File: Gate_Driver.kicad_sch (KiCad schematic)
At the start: 27 parts, among them U1 DRV8323RSRGZR

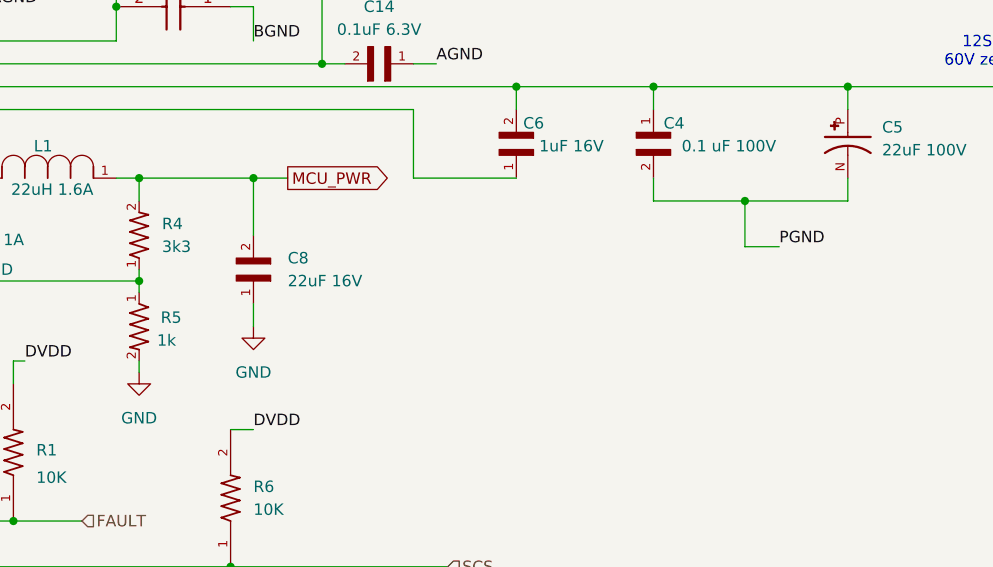
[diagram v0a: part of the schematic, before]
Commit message: Footprints prepared, first pcb project created.
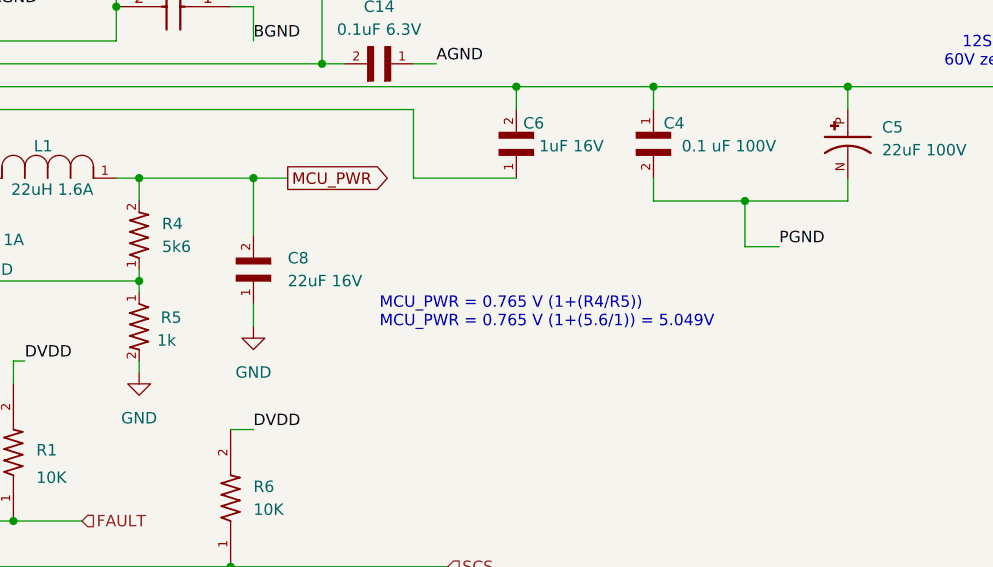
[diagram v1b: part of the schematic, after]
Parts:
- C1, C3: footprint C0805 -> Capacitor_SMD:C_0805_2012Metric_Pad1.18x1.45mm_HandSolder
- C2: footprint CAPC1005X55N -> Capacitor_SMD:C_0603_1608Metric_Pad1.08x0.95mm_HandSolder
- R4: value 3k3 -> 5k6
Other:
- note added: "MCU_PWR = 0.765 V (1+(R4/R5)) MCU_PWR = 0.765 V (1+(5.6/1)) = 5.049V"
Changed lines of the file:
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@@
 		(rev "v0.1")
 	)
+	(text " MCU_PWR = 0.765 V (1+(R4/R5))\n MCU_PWR = 0.765 V (1+(5.6/1)) = 5.049V"
+		(exclude_from_sim no)
+		(at 158.242 74.676 0)
+		(effects
+			(font
+				(size 1.27 1.27)
+			)
+			(justify left)
+		)
+	)
 	(text "MCU must sense the\nvoltage at each phase\nfor 6-step algorithm\n"
 		(exclude_from_sim no)
@@
 			)
 		)
-		(property "Footprint" "CAPC1005X55N"
+		(property "Footprint" "Capacitor_SMD:C_0603_1608Metric_Pad1.08x0.95mm_HandSolder"
 			(at 104.14 -59.36 0)
 			(effects
@@
 			)
 		)
-		(property "Footprint" "C0805"
+		(property "Footprint" "Capacitor_SMD:C_0805_2012Metric_Pad1.18x1.45mm_HandSolder"
 			(at 138.1 121.92 0)
 			(effects
@@
 			)
 		)
-		(property "Footprint" "C0805"
+		(property "Footprint" "Capacitor_SMD:C_0805_2012Metric_Pad1.18x1.45mm_HandSolder"
 			(at 133.35 -55.55 0)
 			(effects
@@
 			)
 		)
-		(property "Value" "3k3"
+		(property "Value" "5k6"
 			(at 134.62 67.3099 90)
 			(effects

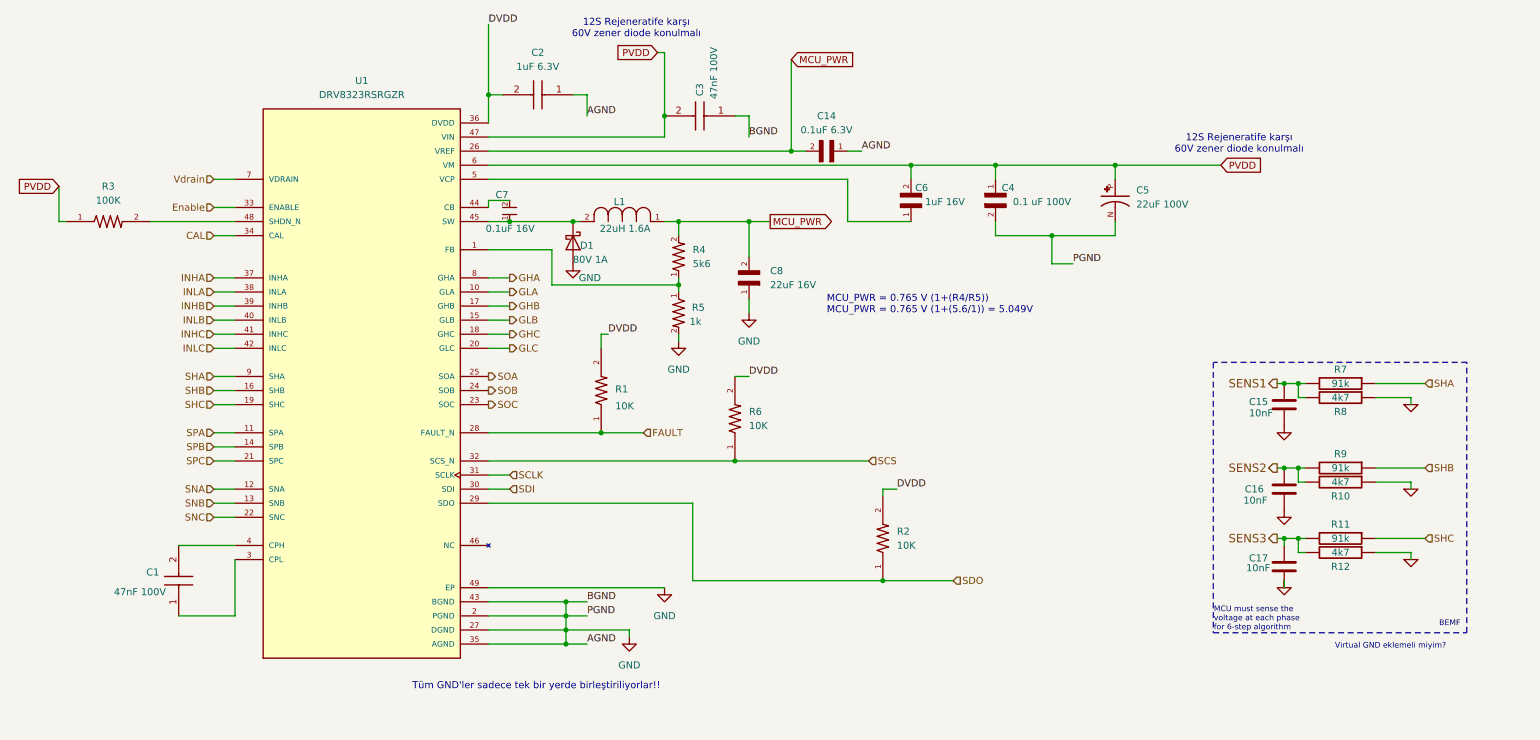
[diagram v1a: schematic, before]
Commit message: component list updated, all footprints updated and now they are compatible to produce with hand (no 0402 size)
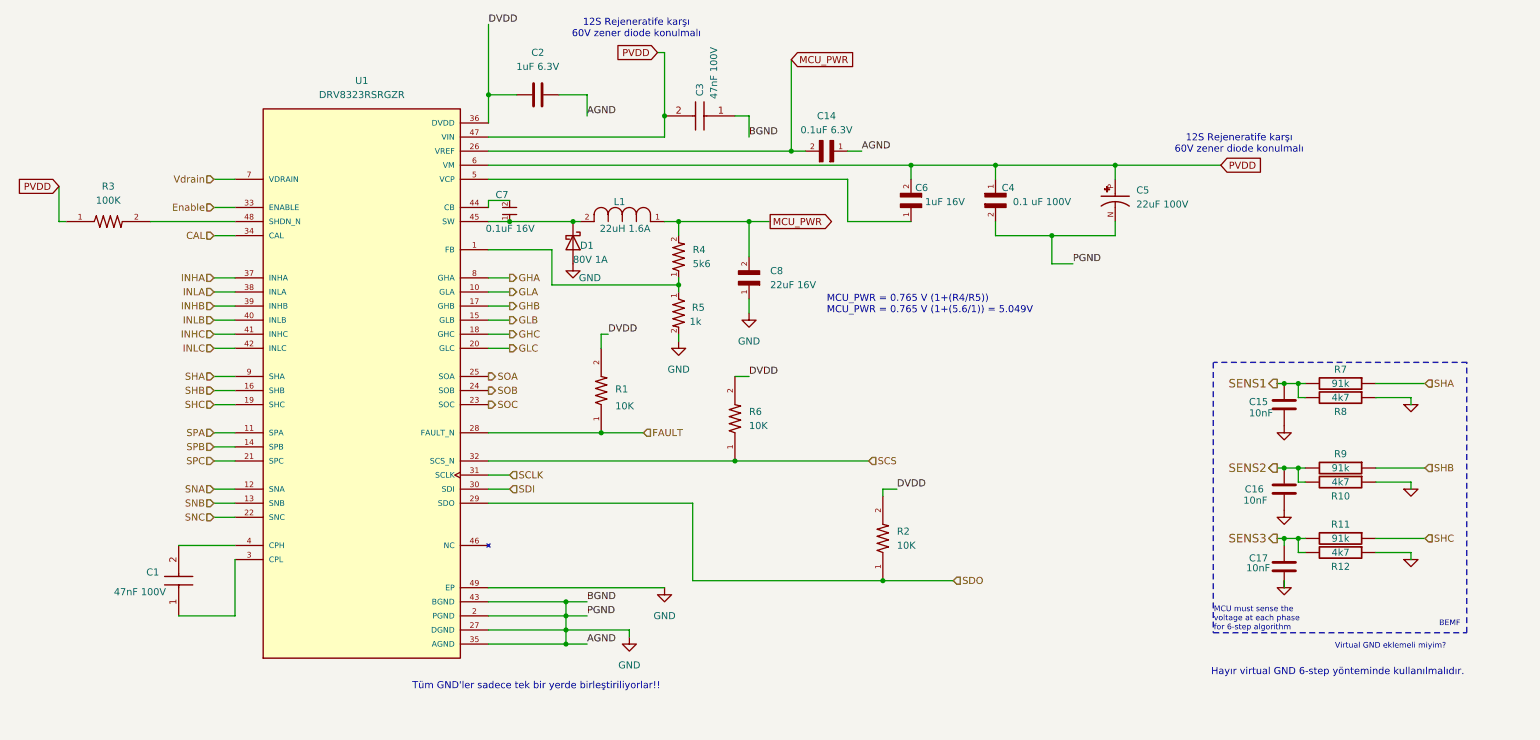
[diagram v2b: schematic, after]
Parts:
- removed C2: 1uF 6.3V, Capacitor_SMD:C_0603_1608Metric_Pad1.08x0.95mm_HandSolder, symbol CL05B105KQ5NQNC:CL05B105KQ5NQNC
- added C2: 1uF 6.3V, Capacitor_SMD:C_0603_1608Metric_Pad1.08x0.95mm_HandSolder, symbol Device:C
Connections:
- net DVDD: now also C2.1
- net GND: now also C2.2
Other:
- note added: "Hayır virtual GND 6-step yönteminde kullanılmalıdır."
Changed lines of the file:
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@@
 		)
 	)
+	(text "Hayır virtual GND 6-step yönteminde kullanılmalıdır."
+		(exclude_from_sim no)
+		(at 250.952 140.97 0)
+		(effects
+			(font
+				(size 1.27 1.27)
+			)
+		)
+	)
 	(text "MCU must sense the\nvoltage at each phase\nfor 6-step algorithm\n"
 		(exclude_from_sim no)
@@
 	(wire
 		(pts
-			(xy 97.79 36.83) (xy 100.33 36.83)
+			(xy 97.79 36.83) (xy 102.87 36.83)
 		)
 		(stroke
@@
 	(wire
 		(pts
-			(xy 113.03 36.83) (xy 115.57 36.83)
-		)
-		(stroke
-			(width 0)
-			(type default)
-		)
-	)
-	(wire
-		(pts
 			(xy 257.81 91.44) (xy 264.16 91.44)
 		)
@@
 	(wire
 		(pts
+			(xy 110.49 36.83) (xy 115.57 36.83)
+		)
+		(stroke
+			(width 0)
+			(type default)
+		)
+	)
+	(wire
+		(pts
 			(xy 48.26 102.87) (xy 52.07 102.87)
 		)
@@
 	)
 	(symbol
-		(lib_id "CL05B105KQ5NQNC:CL05B105KQ5NQNC")
-		(at 113.03 36.83 180)
+		(lib_id "Device:C")
+		(at 106.68 36.83 90)
 		(unit 1)
 		(exclude_from_sim no)
@@
 		(fields_autoplaced yes)
 		(property "Reference" "C2"
-			(at 106.68 29.21 0)
+			(at 106.68 29.21 90)
 			(effects
 				(font
@@
 		)
 		(property "Value" "1uF 6.3V"
-			(at 106.68 31.75 0)
+			(at 106.68 31.75 90)
 			(effects
 				(font
@@
 		)
 		(property "Footprint" "Capacitor_SMD:C_0603_1608Metric_Pad1.08x0.95mm_HandSolder"
-			(at 104.14 -59.36 0)
+			(at 110.49 35.8648 0)
 			(effects
 				(font
 					(size 1.27 1.27)
 				)
-				(justify left top)
 				(hide yes)
 			)
 		)
-		(property "Datasheet" "https://media.digikey.com/pdf/Data%20Sheets/Samsung%20PDFs/CL10A225KO8NNNC_Spec.pdf"
-			(at 104.14 -159.36 0)
+		(property "Datasheet" "https://www.direnc.net/1uf-16v-10-x5r-603-smd-kondansator"
+			(at 106.68 36.83 0)
 			(effects
 				(font
 					(size 1.27 1.27)
 				)
-				(justify left top)
 				(hide yes)
 			)
 		)
-		(property "Description" "Cap Ceramic 1uF 6.3V X7R 10% Pad SMD 0402 125C T/R"
-			(at 113.03 36.83 0)
+		(property "Description" "Unpolarized capacitor ()"
+			(at 106.68 36.83 0)
 			(effects
 				(font
@@
 			)
 		)
-		(property "Height" "0.55"
-			(at 104.14 -359.36 0)
-			(effects
-				(font
-					(size 1.27 1.27)
-				)
-				(justify left top)
-				(hide yes)
-			)
-		)
-		(property "Manufacturer_Name" "SAMSUNG"
-			(at 104.14 -459.36 0)
-			(effects
-				(font
-					(size 1.27 1.27)
-				)
-				(justify left top)
-				(hide yes)
-			)
-		)
-		(property "Manufacturer_Part_Number" "CL05B105KQ5NQNC"
-			(at 104.14 -559.36 0)
-			(effects
-				(font
-					(size 1.27 1.27)
-				)
-				(justify left top)
-				(hide yes)
-			)
-		)
-		(property "Mouser Part Number" "187-CL05B105KQ5NQNC"
-			(at 104.14 -659.36 0)
-			(effects
-				(font
-					(size 1.27 1.27)
-				)
-				(justify left top)
-				(hide yes)
-			)
-		)
-		(property "Mouser Price/Stock" "https://www.mouser.co.uk/ProductDetail/Samsung-Electro-Mechanics/CL05B105KQ5NQNC?qs=rzUXcgKXlodZ31DFWLtHjw%3D%3D"
-			(at 104.14 -759.36 0)
-			(effects
-				(font
-					(size 1.27 1.27)
-				)
-				(justify left top)
-				(hide yes)
-			)
-		)
-		(property "Arrow Part Number" "CL05B105KQ5NQNC"
-			(at 104.14 -859.36 0)
-			(effects
-				(font
-					(size 1.27 1.27)
-				)
-				(justify left top)
-				(hide yes)
-			)
-		)
-		(property "Arrow Price/Stock" "https://www.arrow.com/en/products/cl05b105kq5nqnc/samsung-electro-mechanics?region=nac"
-			(at 104.14 -959.36 0)
-			(effects
-				(font
-					(size 1.27 1.27)
-				)
-				(justify left top)
-				(hide yes)
-			)
-		)
 		(pin "1"
 		)
@@
 			)
 		)
-		(property "Datasheet" ""
+		(property "Datasheet" "kicad-embed://drv8323.pdf"
 			(at 74.93 87.63 0)
 			(effects

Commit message: some tags chaneged, pcb thinked about pcb component placement, aluminum mosfet carrier pcb and paralelling mosfets
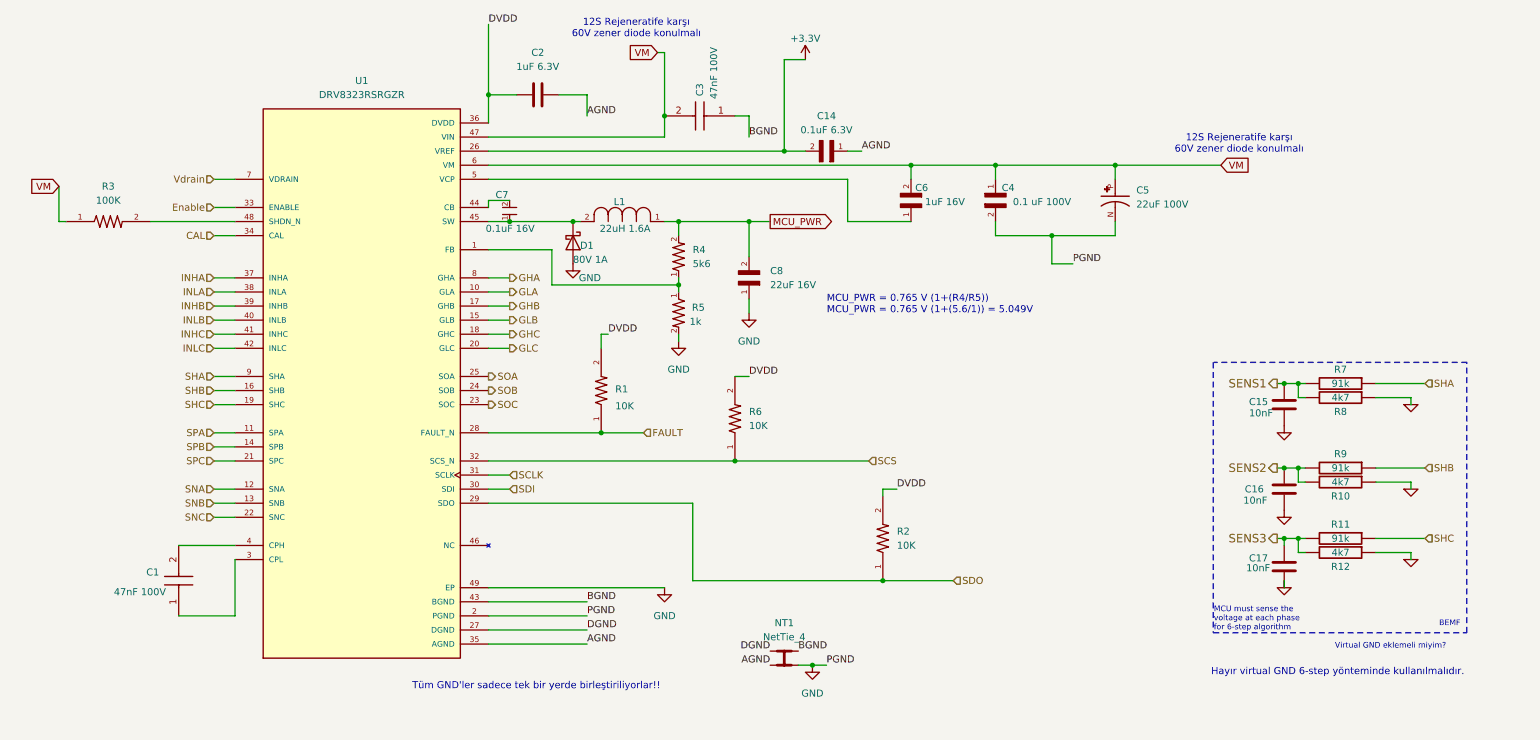
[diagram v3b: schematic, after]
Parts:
- added NT1: NetTie_4, symbol Device:NetTie_4
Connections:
- net GND: now also NT1.4; no longer C14.1, C2.2, C3.1, U1.27 (DGND), U1.35 (AGND), U1.43 (BGND)
- net MCU_PWR: no longer C14.2, U1.26 (VREF)
- net PVDD renamed VM
- new net +3.3V: C14.2, U1.26 (VREF)
- new net AGND: C14.1, C2.2, NT1.3, U1.35 (AGND)
- new net BGND: C3.1, NT1.2, U1.43 (BGND)
- new net DGND: NT1.1, U1.27 (DGND)

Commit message: d;akljadsl;kdsj
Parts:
- C7: footprint CC0603KRX7R7BB104:CAPC1608X90 -> Capacitor_SMD:C_0603_1608Metric_Pad1.08x0.95mm_HandSolder
- C8: footprint CL21A226KOQNNNE:CAPC2012X140N -> Capacitor_SMD:C_0805_2012Metric_Pad1.18x1.45mm_HandSolder
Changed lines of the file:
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@@
 			)
 		)
-		(property "Footprint" "CC0603KRX7R7BB104:CAPC1608X90"
+		(property "Footprint" "Capacitor_SMD:C_0603_1608Metric_Pad1.08x0.95mm_HandSolder"
 			(at 119.888 44.704 0)
 			(effects
@@
 			)
 		)
-		(property "Footprint" "CL21A226KOQNNNE:CAPC2012X140N"
+		(property "Footprint" "Capacitor_SMD:C_0805_2012Metric_Pad1.18x1.45mm_HandSolder"
 			(at 144.78 71.12 0)
 			(effects

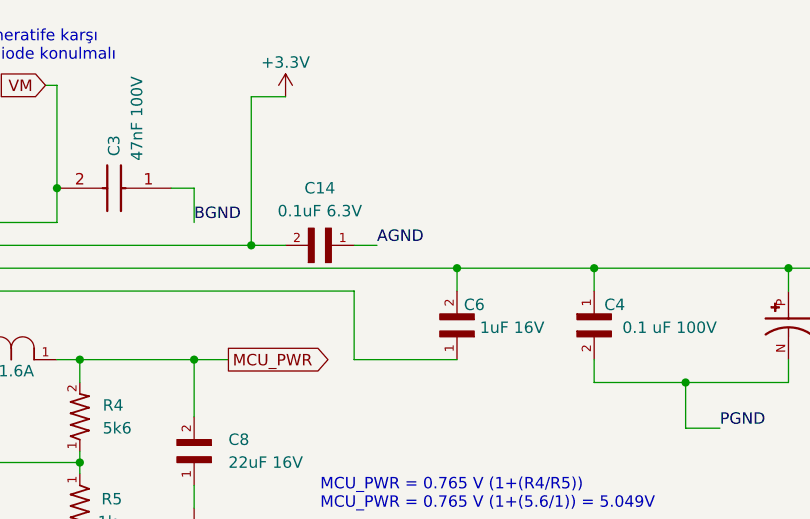
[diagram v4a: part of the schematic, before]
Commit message: started to pcb design, mosfets,shunts drv8323 placement.
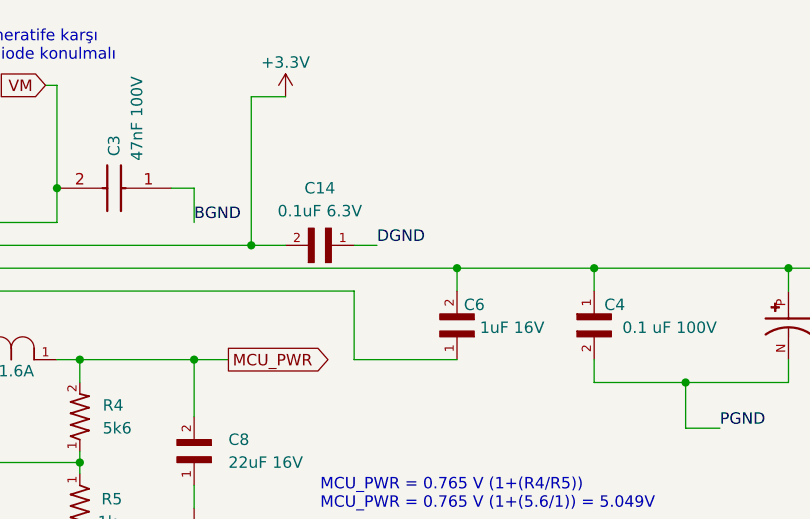
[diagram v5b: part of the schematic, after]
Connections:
- net AGND: no longer C14.1
- net DGND: now also C14.1
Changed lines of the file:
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@@
 		)
 	)
-	(label "AGND"
+	(label "DGND"
 		(at 165.1 46.99 0)
 		(effects

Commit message: all nıght 4/12
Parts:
- removed NT1: NetTie_4, symbol Device:NetTie_4
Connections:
- net GND: no longer C4.2, C5.N, U1.2 (PGND)
- new net PGND: C4.2, C5.N, U1.2 (PGND)
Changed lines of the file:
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@@
 	)
 	(junction
-		(at 156.21 139.7)
-		(diameter 0)
-		(color 0 0 0 0)
-	)
-	(junction
 		(at 243.84 88.9)
 		(diameter 0)
@@
 	(wire
 		(pts
-			(xy 97.79 130.81) (xy 115.57 130.81)
-		)
-		(stroke
-			(width 0)
-			(type default)
-		)
-	)
-	(wire
-		(pts
 			(xy 97.79 72.39) (xy 101.6 72.39)
 		)
@@
 	(wire
 		(pts
-			(xy 97.79 128.27) (xy 115.57 128.27)
-		)
-		(stroke
-			(width 0)
-			(type default)
-		)
-	)
-	(wire
-		(pts
 			(xy 48.26 82.55) (xy 52.07 82.55)
 		)
@@
 		)
 	)
-	(wire
-		(pts
-			(xy 156.21 139.7) (xy 153.67 139.7)
-		)
-		(stroke
-			(width 0)
-			(type default)
-		)
-	)
 	(polyline
 		(pts
@@
 	(wire
 		(pts
+			(xy 97.79 128.27) (xy 115.57 128.27)
+		)
+		(stroke
+			(width 0)
+			(type default)
+		)
+	)
+	(wire
+		(pts
 			(xy 97.79 49.53) (xy 173.99 49.53)
 		)
@@
 	(wire
 		(pts
-			(xy 158.75 139.7) (xy 156.21 139.7)
+			(xy 97.79 130.81) (xy 115.57 130.81)
 		)
 		(stroke
@@
 		)
 	)
-	(label "AGND"
-		(at 148.59 139.7 180)
-		(effects
-			(font
-				(size 1.27 1.27)
-			)
-			(justify right bottom)
-		)
-	)
 	(label "PGND"
 		(at 115.57 130.81 0)
@@
 		)
 	)
-	(label "PGND"
-		(at 158.75 139.7 0)
-		(effects
-			(font
-				(size 1.27 1.27)
-			)
-			(justify left bottom)
-		)
-	)
 	(label "DGND"
 		(at 165.1 46.99 0)
@@
 		)
 	)
-	(label "DGND"
-		(at 148.59 137.16 180)
-		(effects
-			(font
-				(size 1.27 1.27)
-			)
-			(justify right bottom)
-		)
-	)
 	(label "DVDD"
 		(at 171.45 107.95 0)
@@
 		)
 	)
-	(label "BGND"
-		(at 153.67 137.16 0)
-		(effects
-			(font
-				(size 1.27 1.27)
-			)
-			(justify left bottom)
-		)
-	)
 	(global_label "VM"
 		(shape input)
@@
 	)
 	(symbol
-		(lib_id "Device:NetTie_4")
-		(at 151.13 137.16 0)
-		(unit 1)
-		(exclude_from_sim no)
-		(in_bom no)
-		(on_board yes)
-		(dnp no)
-		(fields_autoplaced yes)
-		(property "Reference" "NT1"
-			(at 151.13 132.08 0)
-			(effects
-				(font
-					(size 1.27 1.27)
-				)
-			)
-		)
-		(property "Value" "NetTie_4"
-			(at 151.13 134.62 0)
-			(effects
-				(font
-					(size 1.27 1.27)
-				)
-			)
-		)
-		(property "Footprint" ""
-			(at 151.13 137.16 0)
-			(effects
-				(font
-					(size 1.27 1.27)
-				)
-				(hide yes)
-			)
-		)
-		(property "Datasheet" "~"
-			(at 151.13 137.16 0)
-			(effects
-				(font
-					(size 1.27 1.27)
-				)
-				(hide yes)
-			)
-		)
-		(property "Description" "Net tie, 4 pins"
-			(at 151.13 137.16 0)
-			(effects
-				(font
-					(size 1.27 1.27)
-				)
-				(hide yes)
-			)
-		)
-		(pin "4"
-		)
-		(pin "3"
-		)
-		(pin "2"
-		)
-		(pin "1"
-		)
-		(instances
-			(project ""
-				(path "/57129761-6d47-486c-bd7a-90dbb6f75754/beeab9ba-c868-48bf-b621-5886b9552033"
-					(reference "NT1")
-					(unit 1)
-				)
-			)
-		)
-	)
-	(symbol
 		(lib_id "power:GND")
 		(at 241.3 124.46 0)
@@
 					(unit 1)
 				)
-			)
-		)
-	)
-	(symbol
-		(lib_id "power:GND")
-		(at 156.21 139.7 0)
-		(unit 1)
-		(exclude_from_sim no)
-		(in_bom yes)
-		(on_board yes)
-		(dnp no)
-		(fields_autoplaced yes)
-		(property "Reference" "#PWR09"
-			(at 156.21 146.05 0)
-			(effects
-				(font
-					(size 1.27 1.27)
-				)
-				(hide yes)
-			)
-		)
-		(property "Value" "GND"
-			(at 156.21 144.78 0)
-			(effects
-				(font
-					(size 1.27 1.27)
-				)
-			)
-		)
-		(property "Footprint" ""
-			(at 156.21 139.7 0)
-			(effects
-				(font
-					(size 1.27 1.27)
-				)
-				(hide yes)
-			)
-		)
-		(property "Datasheet" ""
-			(at 156.21 139.7 0)
-			(effects
-				(font
-					(size 1.27 1.27)
-				)
-				(hide yes)
-			)
-		)
-		(property "Description" "Power symbol creates a global label with name \"GND\" , ground"
-			(at 156.21 139.7 0)
-			(effects
-				(font
-					(size 1.27 1.27)
-				)
-				(hide yes)
-			)
-		)
-		(pin "1"
-		)
-		(instances
-			(project "Ana_ESC"
-				(path "/57129761-6d47-486c-bd7a-90dbb6f75754/beeab9ba-c868-48bf-b621-5886b9552033"
-					(reference "#PWR09")
-					(unit 1)
-				)
